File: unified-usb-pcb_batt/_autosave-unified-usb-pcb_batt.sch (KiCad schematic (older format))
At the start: 34 parts, among them J1 QI, J2 USB_C_Receptacle_USB2.0, J3 USB_Out, J4 BATT, J5 THERM, U1 SRV05-4, U2 DW01A, U3 TP4056, U4 FS8205

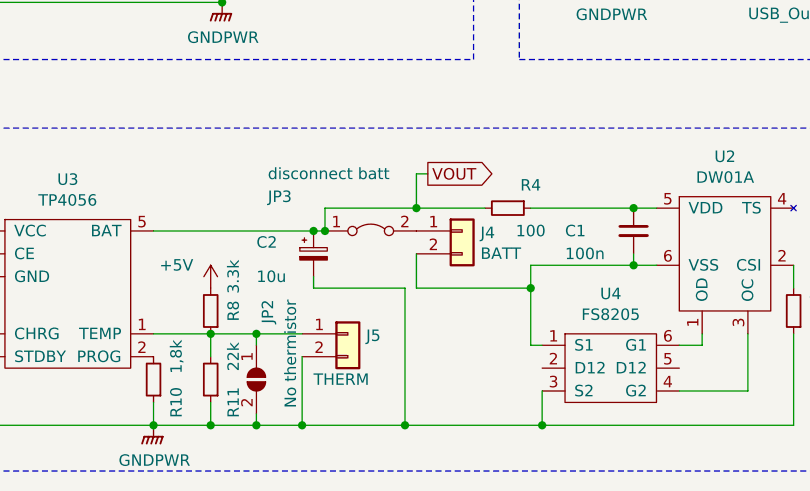
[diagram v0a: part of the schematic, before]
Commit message: continued with Li-Ion schematic, initialised pcb
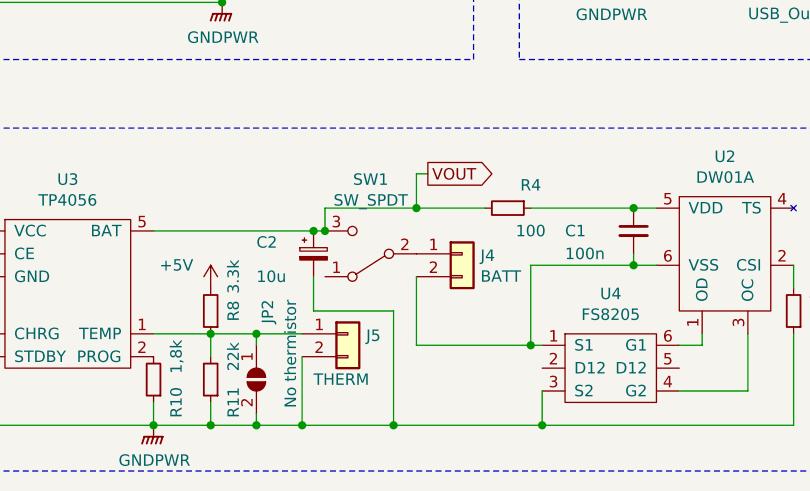
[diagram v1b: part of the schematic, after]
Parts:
- removed JP3: disconnect batt, Connector_PinHeader_2.54mm:PinHeader_1x02_P2.54mm_Vertical, symbol Jumper:Jumper_2_Bridged
- added SW1: SW_SPDT, symbol Switch:SW_SPDT
- C1, C4: footprint Capacitor_Tantalum_SMD:CP_EIA-3216-18_Kemet-A -> Capacitor_SMD:C_0603_1608Metric
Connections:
- net VOUT: now also SW1.3 (C)
- net at J4.1 (Pin_1): now also SW1.2 (B)
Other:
- moved on the sheet: J4
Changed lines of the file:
@@
 USB_D+
-$Comp
-L Connector_Generic:Conn_01x02 J4
-U 1 1 5E8AB5AC
-P 3900 3600
-F 0 "J4" H 3980 3592 50  0000 L CNN
-F 1 "BATT" H 3980 3501 50  0000 L CNN
-F 2 "Connector_JST:JST_SH_SM02B-SRSS-TB_1x02-1MP_P1.00mm_Horizontal" H 3900 3600 50  0001 C CNN
-F 3 "~" H 3900 3600 50  0001 C CNN
-	1    3900 3600
-	1    0    0    -1
-$EndComp
 $Comp
 L Connector_Generic:Conn_01x02 J5
@@
 	3200 4450 3000 4450
 Connection ~ 3000 4450
-Wire Wire Line
-	3700 3700 3700 3850
-Wire Wire Line
-	3700 3850 4200 3850
-Wire Wire Line
-	4200 3850 4200 4100
 $Comp
 L Device:CP_Small C3
@@
 F 0 "C1" H 4350 3600 50  0000 L CNN
 F 1 "100n" H 4350 3500 50  0000 L CNN
-F 2 "Capacitor_Tantalum_SMD:CP_EIA-3216-18_Kemet-A" H 4650 3600 50  0001 C CNN
+F 2 "Capacitor_SMD:C_0603_1608Metric" H 4650 3600 50  0001 C CNN
 F 3 "~" H 4650 3600 50  0001 C CNN
 	1    4650 3600
@@
 Wire Wire Line
 	4650 3750 4200 3750
-Wire Wire Line
-	4200 3750 4200 3850
 Connection ~ 4650 3750
-Connection ~ 4200 3850
 $Comp
 L Device:C_Small C4
@@
 F 0 "C4" V 1550 3650 50  0000 L CNN
 F 1 "100n" V 1550 3800 50  0000 L CNN
-F 2 "Capacitor_Tantalum_SMD:CP_EIA-3216-18_Kemet-A" H 1650 3800 50  0001 C CNN
+F 2 "Capacitor_SMD:C_0603_1608Metric" H 1650 3800 50  0001 C CNN
 F 3 "~" H 1650 3800 50  0001 C CNN
 	1    1650 3800
@@
 	1800 3800 1800 4000
 Wire Wire Line
-	3200 4450 3650 4450
-$Comp
-L Jumper:Jumper_2_Bridged JP3
-U 1 1 5E8F2064
-P 3500 3600
-F 0 "JP3" H 3050 3750 50  0000 L CNN
-F 1 "disconnect batt" H 3050 3850 50  0000 L CNN
-F 2 "Connector_PinHeader_2.54mm:PinHeader_1x02_P2.54mm_Vertical" H 3500 3600 50  0001 C CNN
-F 3 "~" H 3500 3600 50  0001 C CNN
-	1    3500 3600
-	1    0    0    -1
-$EndComp
-Wire Wire Line
-	3250 3800 3250 3850
-Wire Wire Line
-	3250 3850 3650 3850
-Wire Wire Line
-	3650 3850 3650 4450
-Connection ~ 3650 4450
-Wire Wire Line
-	3650 4450 4250 4450
-Wire Wire Line
 	3700 3500 3300 3500
 Wire Wire Line
@@
 Wire Wire Line
 	3300 3600 3250 3600
-Connection ~ 3300 3600
 Wire Wire Line
 	3250 3600 2550 3600
@@
 	3400 2300 3400 1850
 Connection ~ 2350 1900
+$Comp
+L Switch:SW_SPDT SW1
+U 1 1 5E8D451D
+P 3500 3700
+F 0 "SW1" H 3500 3375 50  0000 C CNN
+F 1 "SW_SPDT" H 3500 3466 50  0000 C CNN
+F 2 "" H 3500 3700 50  0001 C CNN
+F 3 "~" H 3500 3700 50  0001 C CNN
+	1    3500 3700
+	-1   0    0    1
+$EndComp
+Connection ~ 3300 3600
+$Comp
+L Connector_Generic:Conn_01x02 J4
+U 1 1 5E8AB5AC
+P 3900 3700
+F 0 "J4" H 3980 3692 50  0000 L CNN
+F 1 "BATT" H 3980 3601 50  0000 L CNN
+F 2 "Connector_JST:JST_SH_SM02B-SRSS-TB_1x02-1MP_P1.00mm_Horizontal" H 3900 3700 50  0001 C CNN
+F 3 "~" H 3900 3700 50  0001 C CNN
+	1    3900 3700
+	1    0    0    -1
+$EndComp
+Wire Wire Line
+	4200 3750 4200 4100
+Wire Wire Line
+	3700 3800 3700 4100
+Wire Wire Line
+	3700 4100 4200 4100
+Connection ~ 4200 4100
+Wire Wire Line
+	3200 4450 3600 4450
+Wire Wire Line
+	3250 3950 3600 3950
+Wire Wire Line
+	3600 3950 3600 4450
+Wire Wire Line
+	3250 3800 3250 3950
+Connection ~ 3600 4450
+Wire Wire Line
+	3600 4450 4250 4450
 $EndSCHEMATC
